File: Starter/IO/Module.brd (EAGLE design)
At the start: 25.4 x 25.4 mm, 2 parts

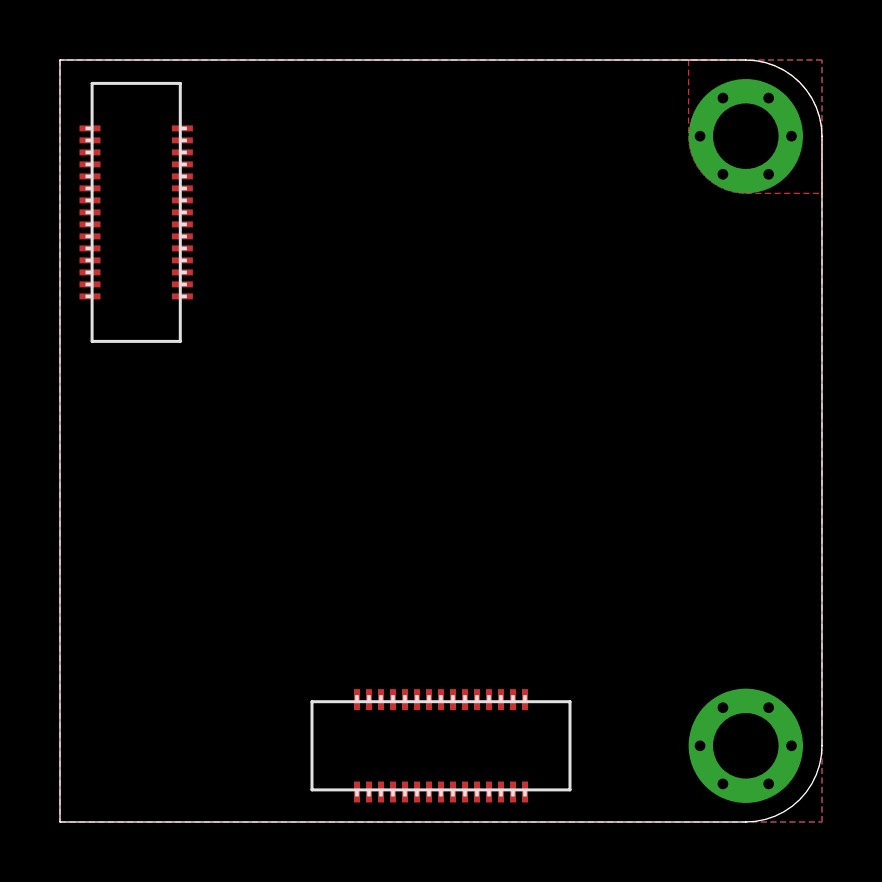
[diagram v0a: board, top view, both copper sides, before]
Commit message: Working on Eagle "parts" for new Root1 scheme
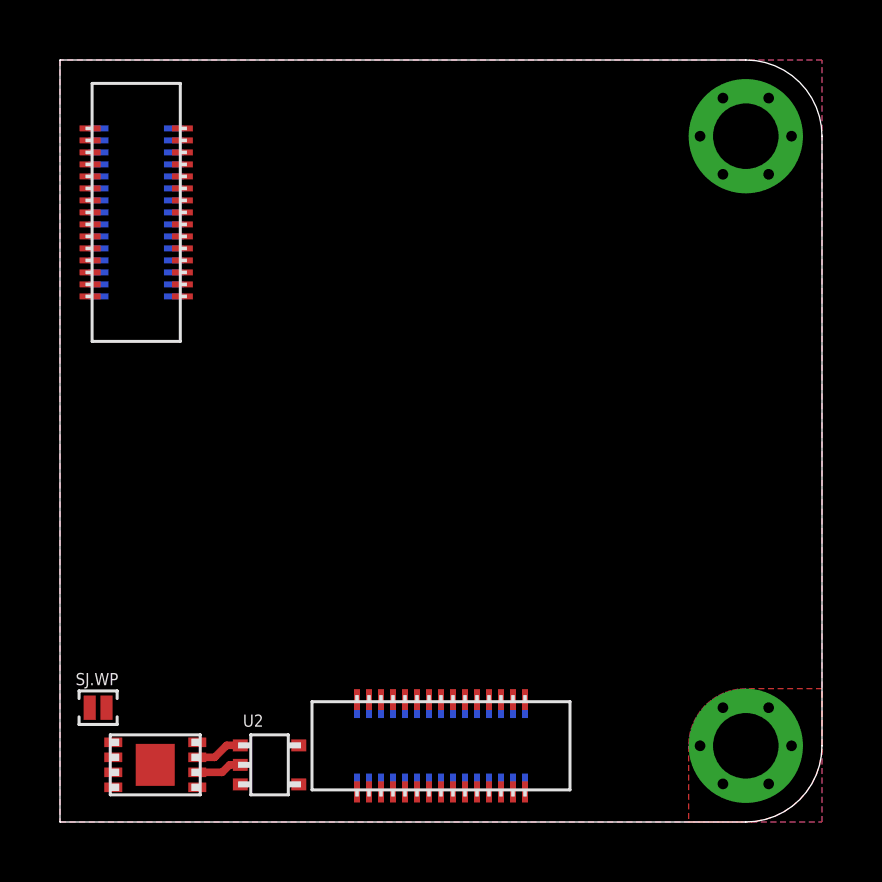
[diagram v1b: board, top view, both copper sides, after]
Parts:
- added J3, J4: DF40.30PIN.HEADER, hirose:DF40(XX)-30DP-0.4V
- added SJ.WP: (no value), solderjumper:2.MED
- added U1: CAT24CXX.UDFN, on-semiconductor:UDFN8.2X3MM
- added U2: NC7S86.SC70-5, fairchild:SC70-5
- renumbered U$8 to J1, U$9 to J2
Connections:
- new net 3.3V: J2.5, J4.1, J4.11, J4.13, J4.15, J4.17, J4.19, J4.21, J4.23, J4.25, J4.3, J4.5, J4.7, J4.9, U1.8, U2.6
- new net A0: J2.3, J4.27, U1.1
- new net A0.NEW: J2.1, J4.29, U2.4
- new net A1: J2.4, J4.28, U1.2, U2.2
- new net A2: J2.2, J4.30, U1.3, U2.1
- new net ADC0: J1.2, J3.30
- new net ADC1: J1.4, J3.28
- new net GND: J1.11, J1.13, J1.15, J1.17, J1.19, J1.21, J1.23, J1.25, J1.27, J1.29, J1.3, J1.5, J1.7, J1.9, J3.1, J3.11, J3.13, J3.15, J3.17, J3.19, J3.21, J3.23, J3.25, J3.27, J3.3, J3.5, J3.7, J3.9, SJ.WP.2, U1.4, U1.PAD, U2.3
- new net IO.0: J1.16, J3.16
- new net IO.1: J1.18, J3.14
- new net IO.2: J1.20, J3.12
- new net IO.3: J1.22, J3.10
- new net IO.4: J1.24, J3.8
- new net IO.5: J1.26, J3.6
- new net IO.6: J1.28, J3.4
- new net IO.7: J1.30, J3.2
- new net MISO: J1.12, J3.20
- new net MOSI: J1.10, J3.22
- new net N$1: SJ.WP.1, U1.7
- new net N$2: J2.11, J2.13, J2.15, J2.17, J2.19, J2.21, J2.23, J2.25, J2.27, J2.29, J2.7, J2.9
- new net N/C.0: J2.24, J4.8
- new net N/C.1: J2.26, J4.6
- new net N/C.2: J2.28, J4.4
- new net N/C.3: J2.30, J4.2
- new net RES.0: J2.14, J4.18
- new net RES.1: J2.16, J4.16
- new net RES.2: J2.18, J4.14
- new net RES.3: J2.20, J4.12
- new net RES.4: J2.22, J4.10
- new net RST: J1.1
- new net RXI: J1.8, J3.24
- new net RXI.DBG: J2.12, J4.20
- new net SCL: J2.8, J4.24, U1.6
- new net SCLK: J1.14, J3.18
- new net SDA: J2.6, J4.26, U1.5
- new net TXO: J1.6, J3.26
- new net TXO.DBG: J2.10, J4.22
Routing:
- net A2: track 0.00 -> 1.60 mm
- net A1: track 0.00 -> 1.54 mm
